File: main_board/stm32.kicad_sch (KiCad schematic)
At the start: 0 parts

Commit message: sch: update sch
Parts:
- added U7: STM32WB55RGVx, Package_DFN_QFN:QFN-68-1EP_8x8mm_P0.4mm_EP6.4x6.4mm, symbol MCU_ST_STM32WB:STM32WB55RGVx
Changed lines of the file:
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@@
 	(generator_version "8.0")
 	(paper "A4")
+	(symbol
+		(lib_id "MCU_ST_STM32WB:STM32WB55RGVx")
+		(at 140.97 102.87 0)
+		(unit 1)
+		(exclude_from_sim no)
+		(in_bom yes)
+		(on_board yes)
+		(dnp no)
+		(fields_autoplaced yes)
+		(property "Reference" "U7"
+			(at 148.2441 148.59 0)
+			(effects
+				(font
+					(size 1.27 1.27)
+				)
+				(justify left)
+			)
+		)
+		(property "Value" "STM32WB55RGVx"
+			(at 148.2441 151.13 0)
+			(effects
+				(font
+					(size 1.27 1.27)
+				)
+				(justify left)
+			)
+		)
+		(property "Footprint" "Package_DFN_QFN:QFN-68-1EP_8x8mm_P0.4mm_EP6.4x6.4mm"
+			(at 123.19 146.05 0)
+			(effects
+				(font
+					(size 1.27 1.27)
+				)
+				(justify right)
+				(hide yes)
+			)
+		)
+		(property "Datasheet" "https://www.st.com/resource/en/datasheet/stm32wb55rg.pdf"
+			(at 140.97 102.87 0)
+			(effects
+				(font
+					(size 1.27 1.27)
+				)
+				(hide yes)
+			)
+		)
+		(property "Description" "STMicroelectronics Arm Cortex-M4 MCU, 1024KB flash, 256KB RAM, 64 MHz, 1.71-3.6V, 49 GPIO, VFQFPN68"
+			(at 140.97 102.87 0)
+			(effects
+				(font
+					(size 1.27 1.27)
+				)
+				(hide yes)
+			)
+		)
+		(pin "53"
+		)
+		(pin "6"
+		)
+		(pin "35"
+		)
+		(pin "54"
+		)
+		(pin "59"
+		)
+		(pin "56"
+		)
+		(pin "55"
+		)
+		(pin "57"
+		)
+		(pin "58"
+		)
+		(pin "34"
+		)
+		(pin "19"
+		)
+		(pin "12"
+		)
+		(pin "3"
+		)
+		(pin "64"
+		)
+		(pin "24"
+		)
+		(pin "22"
+		)
+		(pin "33"
+		)
+		(pin "60"
+		)
+		(pin "11"
+		)
+		(pin "21"
+		)
+		(pin "67"
+		)
+		(pin "20"
+		)
+		(pin "16"
+		)
+		(pin "49"
+		)
+		(pin "32"
+		)
+		(pin "68"
+		)
+		(pin "13"
+		)
+		(pin "23"
+		)
+		(pin "38"
+		)
+		(pin "37"
+		)
+		(pin "17"
+		)
+		(pin "31"
+		)
+		(pin "15"
+		)
+		(pin "50"
+		)
+		(pin "14"
+		)
+		(pin "61"
+		)
+		(pin "30"
+		)
+		(pin "48"
+		)
+		(pin "8"
+		)
+		(pin "27"
+		)
+		(pin "9"
+		)
+		(pin "43"
+		)
+		(pin "1"
+		)
+		(pin "42"
+		)
+		(pin "62"
+		)
+		(pin "5"
+		)
+		(pin "69"
+		)
+		(pin "36"
+		)
+		(pin "29"
+		)
+		(pin "28"
+		)
+		(pin "63"
+		)
+		(pin "47"
+		)
+		(pin "45"
+		)
+		(pin "26"
+		)
+		(pin "7"
+		)
+		(pin "2"
+		)
+		(pin "41"
+		)
+		(pin "46"
+		)
+		(pin "25"
+		)
+		(pin "51"
+		)
+		(pin "66"
+		)
+		(pin "10"
+		)
+		(pin "40"
+		)
+		(pin "44"
+		)
+		(pin "39"
+		)
+		(pin "65"
+		)
+		(pin "18"
+		)
+		(pin "4"
+		)
+		(pin "52"
+		)
+		(instances
+			(project ""
+				(path "/16216a68-6dea-41d7-8e15-2cc84f72f8e2/8225a072-bd5c-4ab0-988a-5acfd87a3b3a"
+					(reference "U7")
+					(unit 1)
+				)
+			)
+		)
+	)
 )

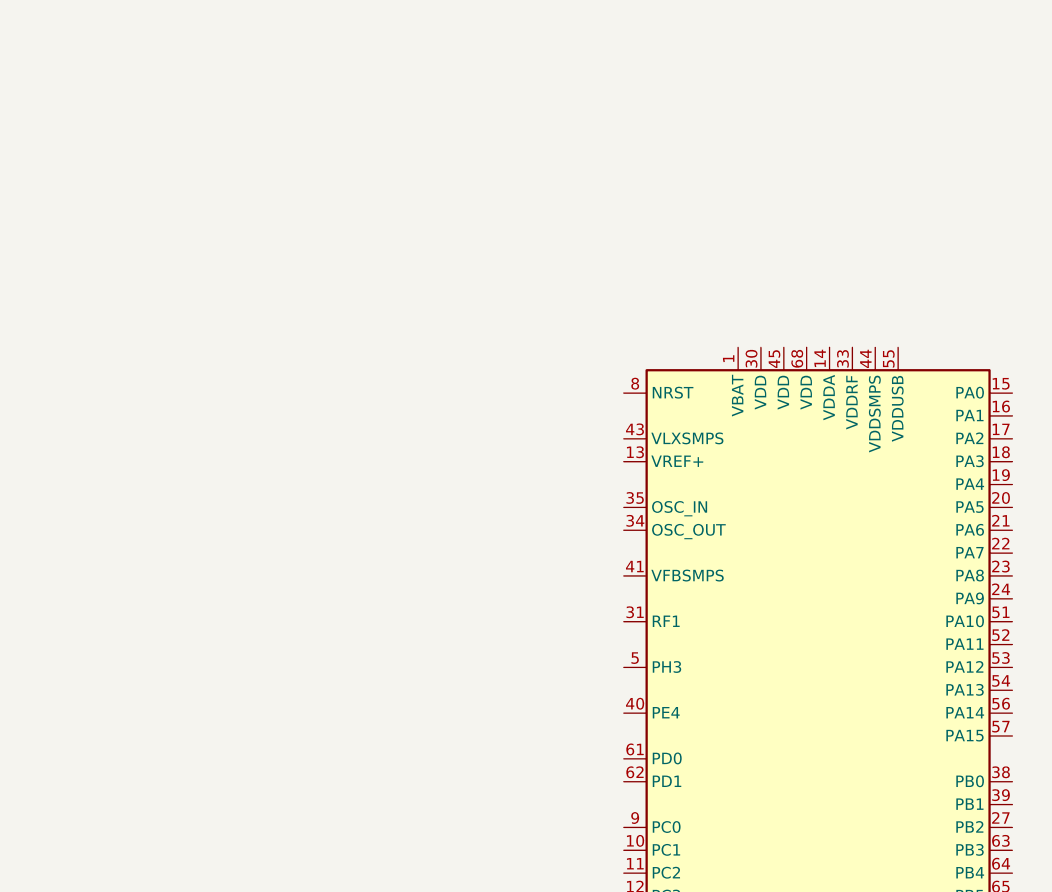
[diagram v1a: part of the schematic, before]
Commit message: sch: working on stm32wb55
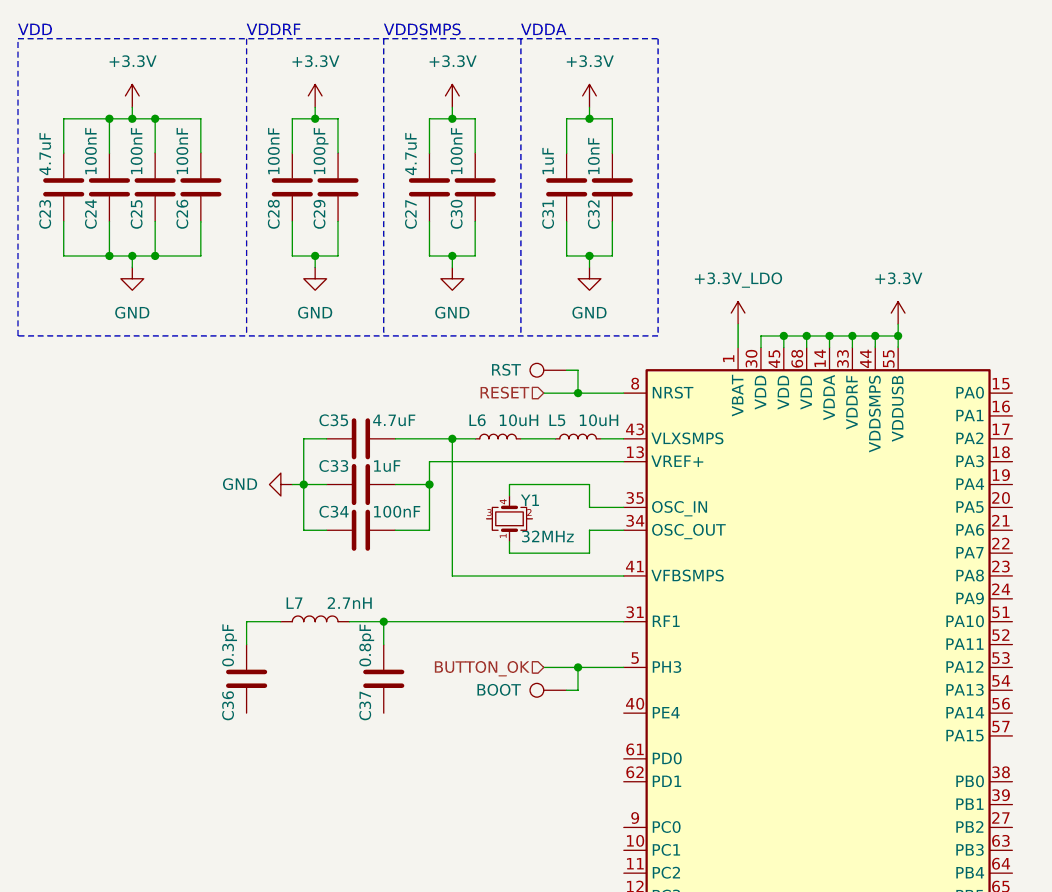
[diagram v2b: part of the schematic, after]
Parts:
- added C23, C27, C35: 4.7uF, symbol Device:C
- added C24, C25, C26, C28, C30, C34: 100nF, symbol Device:C
- added C29: 100pF, symbol Device:C
- added C31, C33: 1uF, symbol Device:C
- added C32: 10nF, symbol Device:C
- added C36: 0.3pF, symbol Device:C
- added C37: 0.8pF, symbol Device:C
- added L5, L6: 10uH, symbol Device:L_Small
- added L7: 2.7nH, symbol Device:L
- added TP21: RST, symbol Connector:TestPoint
- added TP23: BOOT, symbol Connector:TestPoint
- added Y1: 32MHz, symbol Device:Crystal_GND23_Small
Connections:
- net +3.3V_LDO: now reaches U7.1 (VBAT)
- net at U7.13 (VREF+): now also C33.2, C34.2
- net +3.3V: now reaches U7.14 (VDDA)
- net +3.3V: now also U7.30 (VDD), U7.33 (VDDRF), U7.44 (VDDSMPS), U7.45 (VDD), U7.55 (VDDUSB), U7.68 (VDD), C23.2, C24.2, C25.2, C26.2, C27.2, C28.2, C29.2, C30.2, C31.2, C32.2
- net at U7.31 (RF1): now also C37.2, L7.2
- net at U7.34 (OSC_OUT): now also Y1.1
- net at U7.35 (OSC_IN): now also Y1.4
- net at U7.41 (VFBSMPS): now also C35.2, L6.1
- net at U7.43 (VLXSMPS): now also L5.2
- net BUTTON_OK: now reaches U7.5 (PH3)
- net BUTTON_OK: now also TP23.1
- net RESET: now reaches U7.8 (NRST)
- net RESET: now also TP21.1
- new net: C36.2, L7.1
- new net: L5.1, L6.2
- new net GND: C23.1, C24.1, C25.1, C26.1, C27.1, C28.1, C29.1, C30.1, C31.1, C32.1, C33.1, C34.1, C35.1
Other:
- note added: "VDD"
- note added: "VDDA"
- note added: "VDDRF"
- note added: "VDDSMPS"

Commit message: sch: done stm32wb55
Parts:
- added AE1: CrossAir, symbol Device:Antenna_Chip
- added C38, C39: 18pF, symbol Device:C
- added FL1: SAFEA2G45MC0F0A, Filter:Filter_1411-5_1.4x1.1mm, symbol Library:SAFEA2G45MC0F0A
- added R15: 51R, symbol Device:R_US
- added TP24: D_SCK, symbol Connector:TestPoint
- added TP25: D_MISO, symbol Connector:TestPoint
- added TP26: R_SCK, symbol Connector:TestPoint
- added TP27: DM, symbol Connector:TestPoint
- added TP28: DP, symbol Connector:TestPoint
- added TP29: R_MISO, symbol Connector:TestPoint
- added TP30: R_MOSI, symbol Connector:TestPoint
- added TP31: D_MOSI, symbol Connector:TestPoint
- added Y2: 32.768K, symbol Device:Crystal
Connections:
- net GND: now also C36.1, C37.1, U7.32 (VSSRF), U7.42 (VSSSMPS), U7.69 (VSS), Y1.2, Y1.3, AE1.2 (PCB_Trace), C38.1, C39.1, FL1.2 (GND), FL1.3 (GND), FL1.5 (GND), FL1.6 (GND)
- net at C36.2, L7.1: now also FL1.1 (IN)
- net PC1: now reaches U7.10 (PC1)
- net SPI_D_MISO: now reaches U7.11 (PC2)
- net SPI_D_MISO: now also TP25.1
- net PC3: now reaches U7.12 (PC3)
- net IR_RX: now reaches U7.15 (PA0)
- net CC1101_G0: now reaches U7.16 (PA1)
- net RFID_PULL: now reaches U7.17 (PA2)
- net PERI_EN: now reaches U7.18 (PA3)
- net PA4: now reaches U7.19 (PA4)
- net BUTTON_BACK: now reaches U7.2 (PC13)
- net SPI_R_SCK: now reaches U7.20 (PA5)
- net SPI_R_SCK: now also TP26.1
- net PA6: now reaches U7.21 (PA6)
- net PA7: now reaches U7.22 (PA7)
- net VIBRO: now reaches U7.23 (PA8)
- net I2C_SCL: now reaches U7.24 (PA9)
- net RF_SW_0: now reaches U7.25 (PC4)
- net RFID_RF_IN: now reaches U7.26 (PC5)
- net PB2: now reaches U7.27 (PB2)
- net BUTTON_UP: now reaches U7.28 (PB10)
- net BUTTON_LEFT: now reaches U7.29 (PB11)
- net at U7.3 (PC14): now also C38.2, Y2.2
- net DISPLAY_RST: now reaches U7.38 (PB0)
- net DISPLAY_DI: now reaches U7.39 (PB1)
- net at U7.4 (PC15): now also C39.2, Y2.1
- net NFC_CE: now reaches U7.40 (PE4)
- net BUTTON_RIGHT: now reaches U7.46 (PB12)
- net RFID_OUT: now reaches U7.47 (PB13)
- net iBTN: now reaches U7.48 (PB14)
- net SPI_D_MOSI: now reaches U7.49 (PB15)
- net SPI_D_MOSI: now also TP31.1
- net BUTTON_DOWN: now reaches U7.50 (PC6)
- net I2C_SDA: now reaches U7.51 (PA10)
- net D-: now reaches U7.52 (PA11)
- net D-: now also TP27.1
- net D+: now reaches U7.53 (PA12)
- net D+: now also TP28.1
- net SWDIO: now reaches U7.54 (PA13)
- net SWCLK: now reaches U7.56 (PA14)
- net RFID_CARRIER: now reaches U7.57 (PA15)
- net SD_CD: now reaches U7.58 (PC10)
- net DISPLAY_CS: now reaches U7.59 (PC11)
- net SPEAKER: now reaches U7.6 (PB8)
- net SD_CS: now reaches U7.60 (PC12)
- net CC1101_CS: now reaches U7.61 (PD0)
- net SPI_D_SCK: now reaches U7.62 (PD1)
- net SPI_D_SCK: now also TP24.1
- net PB3: now reaches U7.63 (PB3)
- net SPI_R_MISO: now reaches U7.64 (PB4)
- net SPI_R_MISO: now also TP29.1
- net at U7.65 (PB5): now also R15.1
- net UART1_TX: now reaches U7.66 (PB6)
- net UART1_RX: now reaches U7.67 (PB7)
- net IR_TX: now reaches U7.7 (PB9)
- net PC0: now reaches U7.9 (PC0)
- new net: AE1.1 (FEED), FL1.4 (OUT)
- new net SPI_R_MOSI: R15.2, TP30.1
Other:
- moved on the sheet: C23, C24, C25, C26, C27, C28, C29, C30, C31, C32, C33, C34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
